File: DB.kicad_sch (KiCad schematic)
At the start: 20 parts

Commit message: Second Commit
new wiring and label
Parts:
- removed DBP0: Conn_01x11_Pin, symbol Connector:Conn_01x11_Pin
- removed DBP1 (x2): Conn_01x05_Pin, symbol Connector:Conn_01x05_Pin
- removed DBS0: Conn_01x11_Socket, Connector_Molex:Molex_PicoBlade_53261-1171_1x11-1MP_P1.25mm_Horizontal, symbol Connector:Conn_01x11_Socket
- removed DBS1: Conn_01x05_Socket, Connector_Molex:Molex_PicoBlade_53261-0571_1x05-1MP_P1.25mm_Horizontal, symbol Connector:Conn_01x05_Socket
- removed R1, R2 (x2): 5.1K, ScottoKeebs_Components:Resistor_0402, symbol Device:R_Small
- removed RK1: RotaryEncoder_Switch_MP, Rotary_Encoder:RotaryEncoder_Alps_EC11E-Switch_Vertical_H20mm, symbol Device:RotaryEncoder_Switch_MP
- removed SSW1 (x2): MSK13C01, Button_Switch_SMD:SW_SP3T_PCM13, symbol Switch:SW_SP3T
- removed SSW2 (x2): MSK12C01, Button_Switch_SMD:SW_SPDT_PCM12, symbol Switch:SW_SPDT
- removed USB1 (x2): USB_C_Receptacle_USB2.0_14P, ScottoKeebs_Components:USB_C_HRO_TYPE-C-31-M-12, symbol Connector:USB_C_Receptacle_USB2.0_14P
- added DBP1: Conn_01x05_Pin, symbol Connector:Conn_01x05_Pin
- added R2: 5.1K, ScottoKeebs_Components:Resistor_0402, symbol Device:R_Small
- added SSW1: MSK13C01, Button_Switch_SMD:SW_SP3T_PCM13, symbol Switch:SW_SP3T
- added SSW2: MSK12C01, Button_Switch_SMD:SW_SPDT_PCM12, symbol Switch:SW_SPDT
- added USB1: USB_C_Receptacle_USB2.0_14P, ScottoKeebs_Components:USB_C_HRO_TYPE-C-31-M-12, symbol Connector:USB_C_Receptacle_USB2.0_14P
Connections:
- net 2.4GHz Switch: now also SSW1.4
- net BT Switch: now also SSW1.1
- net COM Mode: now also SSW1.3
- net COM OS: now also SSW2.2 (B)
- net COM RK DBS: now also DBP1.3 (Pin_3)
- net GND: now also R2.2, USB1.A1 (GND), USB1.A12 (GND), USB1.B1 (GND), USB1.B12 (GND), USB1.S1 (SHIELD)
- net S1 RK DBS: now also DBP1.2 (Pin_2)
- net S2 RK DBS: now also DBP1.4 (Pin_4)
- net USB CC1: now also USB1.A5 (CC1)
- net USB CC2: now also R2.1, USB1.B5 (CC2)
- net USB D+: now also USB1.A6 (D+), USB1.B6 (D+)
- net USB D-: now also USB1.A7 (D-), USB1.B7 (D-)
- net VBUS: now also USB1.A4 (VBUS), USB1.A9 (VBUS), USB1.B4 (VBUS), USB1.B9 (VBUS)
- net VOL DOWN DBS: now also DBP1.1 (Pin_1)
- net VOL UP DBS: now also DBP1.5 (Pin_5)
- net Win: now also SSW2.1 (A)

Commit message: Third Commit
Kinda add some little changes but still confused on how using the nPM1300
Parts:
- removed RK1: RotaryEncoder_Switch_MP, Rotary_Encoder:RotaryEncoder_Alps_EC11E-Switch_Vertical_H20mm, symbol Device:RotaryEncoder_Switch_MP
- added RK1: RotaryEncoder_Switch_MP, HE_Keyswitch:RotaryEncoder_Bourns_Vertical_PEC11J-9220F-S0015, symbol HE_Keyswitch:RotaryEncoder_Switch_MP
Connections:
- net COM RK: now also RK1.C
- net S1 RK: now also DBS1.4 (Pin_4), RK1.D; no longer DBS1.2 (Pin_2)
- net S2 RK: now also DBS1.2 (Pin_2), RK1.E (S2); no longer DBS1.4 (Pin_4)
- net USB CC1: now also DBS0.9 (Pin_9); no longer DBS0.11 (Pin_11)
- net USB CC1 DBS: now also DBP0.9 (Pin_9); no longer DBP0.11 (Pin_11)
- net USB D+: now also DBS0.10 (Pin_10); no longer DBS0.9 (Pin_9)
- net USB D+ DBS: now also DBP0.10 (Pin_10); no longer DBP0.9 (Pin_9)
- net USB D-: now also DBS0.11 (Pin_11); no longer DBS0.10 (Pin_10)
- net USB D- DBS: now also DBP0.11 (Pin_11); no longer DBP0.10 (Pin_10)
- net VOL DOWN: now also RK1.B
- net VOL UP: now also RK1.A

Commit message: Fourth Commit
changing some name to not get sued :v
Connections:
- net USB CC1 DBS is gone; now on net Win DBS: DBP0.9 (Pin_9)
- net USB CC2 DBS is gone; now on net COM OS DBS: DBP0.8 (Pin_8)
- net COM OS: now also DBS0.8 (Pin_8); no longer DBS0.4 (Pin_4)
- net COM OS DBS: no longer DBP0.4 (Pin_4)
- net COM RK: now also DBS1.4 (Pin_4); no longer DBS1.3 (Pin_3)
- net COM RK DBS: now also DBP1.4 (Pin_4); no longer DBP1.3 (Pin_3)
- net GND: now also DBP0.4 (Pin_4), DBS0.4 (Pin_4); no longer DBP0.6 (Pin_6), DBS0.6 (Pin_6)
- net S1 RK: now also DBS1.2 (Pin_2); no longer DBS1.4 (Pin_4)
- net S2 RK: now also DBS1.1 (Pin_1); no longer DBS1.2 (Pin_2)
- net S2 RK DBS: now also DBP1.1 (Pin_1); no longer DBP1.4 (Pin_4)
- net USB CC1: now also DBS0.7 (Pin_7); no longer DBS0.9 (Pin_9)
- net USB CC2: now also DBS0.6 (Pin_6); no longer DBS0.8 (Pin_8)
- net VBUS: now also DBS0.5 (Pin_5); no longer DBS0.7 (Pin_7)
- net VBUS DBS: now also DBP0.5 (Pin_5); no longer DBP0.7 (Pin_7)
- net VOL DOWN: now also DBS1.5 (Pin_5); no longer DBS1.1 (Pin_1)
- net VOL DOWN DBS: now also DBP1.5 (Pin_5); no longer DBP1.1 (Pin_1)
- net VOL UP: now also DBS1.3 (Pin_3); no longer DBS1.5 (Pin_5)
- net VOL UP DBS: now also DBP1.3 (Pin_3); no longer DBP1.5 (Pin_5)
- net Win: now also DBS0.9 (Pin_9); no longer DBS0.5 (Pin_5)
- net Win DBS: no longer DBP0.5 (Pin_5)
- net USB D+ DBS renamed D+ DBS
- net USB D- DBS renamed D- DBS
- new net CC1 DBS: DBP0.7 (Pin_7)
- new net CC2 DBS: DBP0.6 (Pin_6)

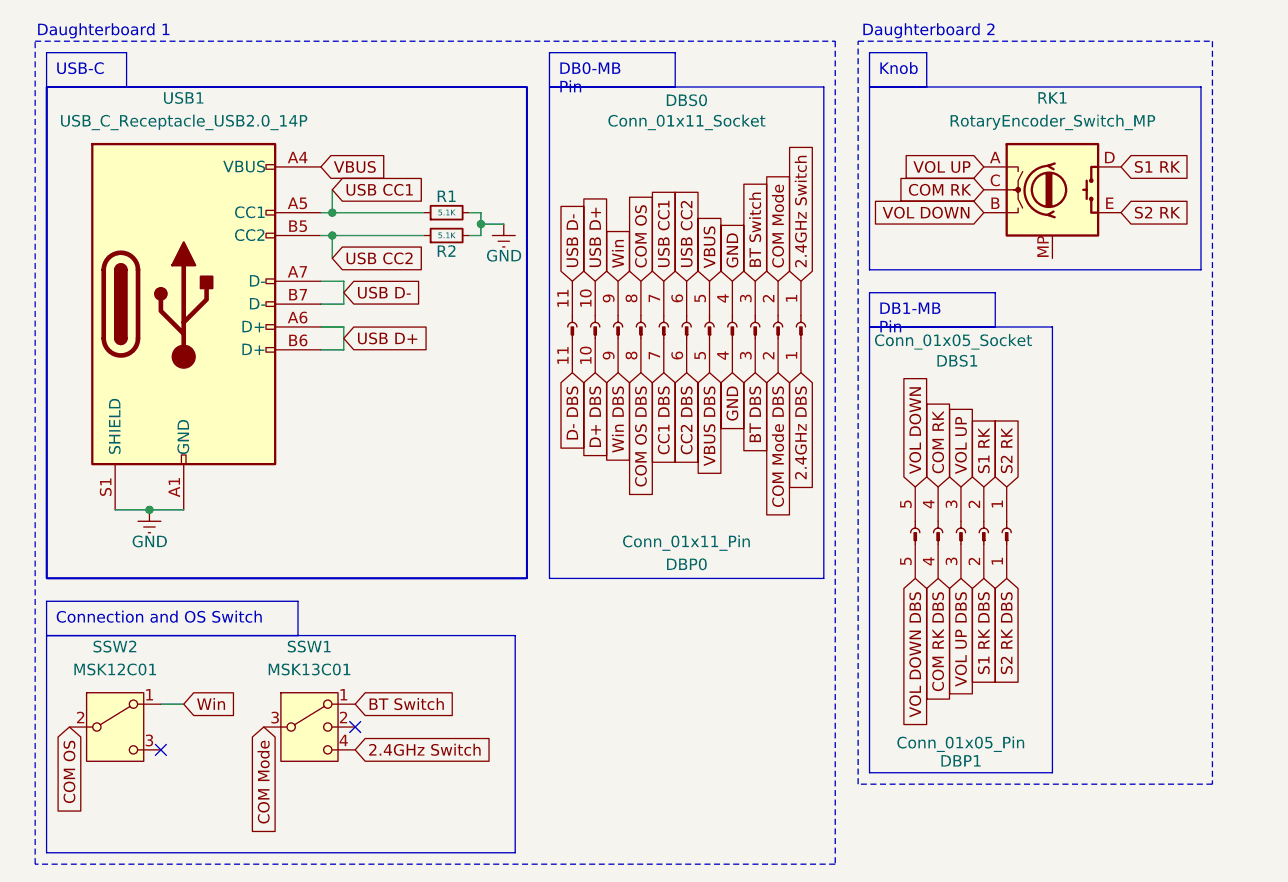
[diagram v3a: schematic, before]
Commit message: Fifth Commit
updating track width and via's diameter
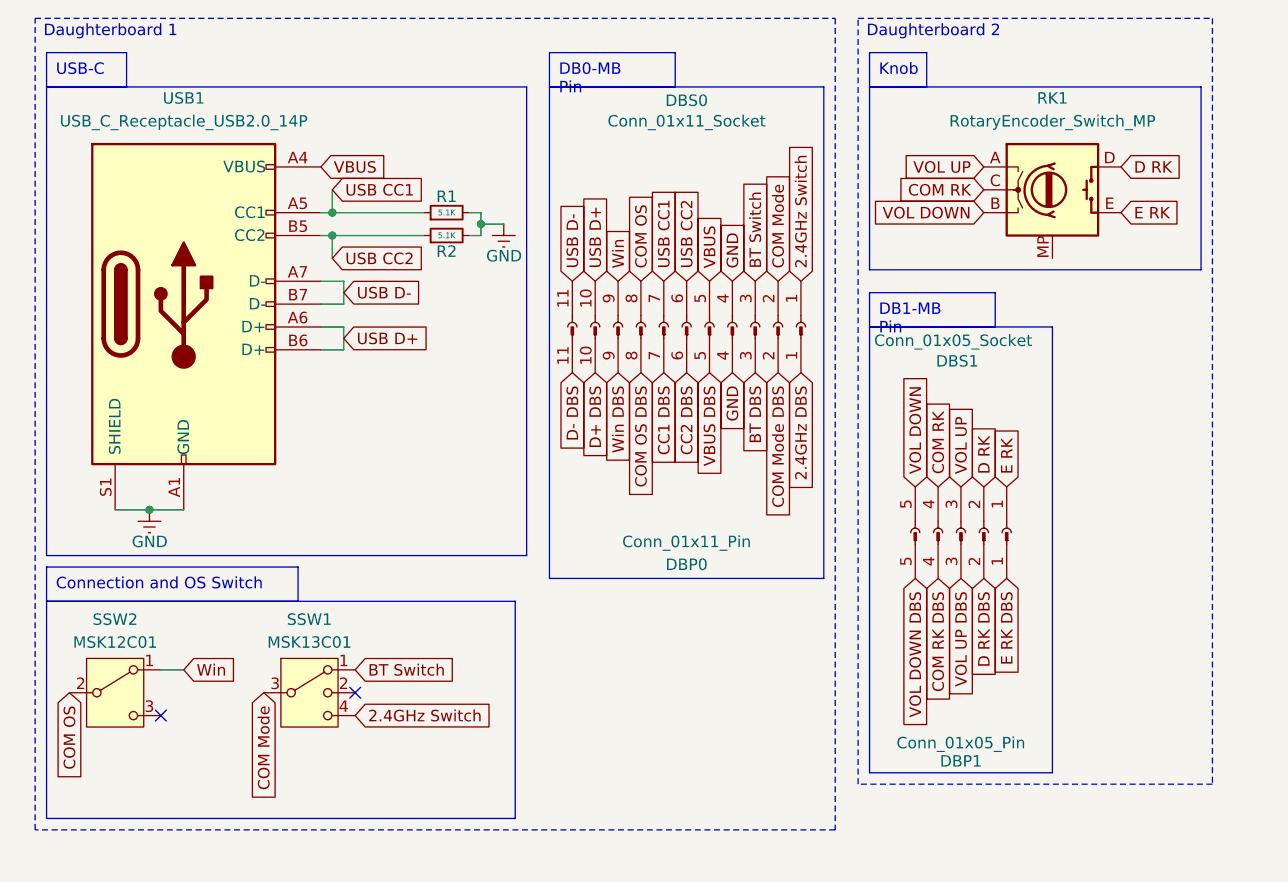
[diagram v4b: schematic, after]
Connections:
- net S1 RK renamed D RK
- net S1 RK DBS renamed D RK DBS
- net S2 RK renamed E RK
- net S2 RK DBS renamed E RK DBS
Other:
- moved on the sheet: SSW1, SSW2

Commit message: Sixth Commit
Almost done. Just need to make sure the field zone and each pin is connected properly
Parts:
- removed R1, R2: 5.1K, ScottoKeebs_Components:Resistor_0402, symbol Device:R_Small
- J1: renamed from USB1; symbol Connector:USB_C_Receptacle_USB2.0_14P -> HE_Keyswitch:USB_C_Receptacle_USB2.0_14P
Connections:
- net COM RK is gone; now on net GND: DBS1.4 (Pin_4), RK1.C
- net E RK is gone; now on net GND: DBS1.1 (Pin_1), RK1.E (S2)
- net VBUS DBS is gone; now on net CC2 DBS: DBP0.5 (Pin_5)
- net CC1 DBS: now also DBP0.6 (Pin_6); no longer DBP0.7 (Pin_7)
- net CC2 DBS: no longer DBP0.6 (Pin_6)
- net USB CC1: now also DBS0.6 (Pin_6); no longer DBS0.7 (Pin_7)
- net USB CC2: now also DBS0.5 (Pin_5); no longer DBS0.6 (Pin_6)
- net VBUS: now also DBP0.7 (Pin_7), DBS0.7 (Pin_7); no longer DBS0.5 (Pin_5)
- net MP: now reaches RK1.MP
- net D+ DBS renamed DBS D+
- net D- DBS renamed DBS D-
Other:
- moved on the sheet: DBP0, DBP1, DBS0, DBS1, J1, RK1, SSW1, SSW2

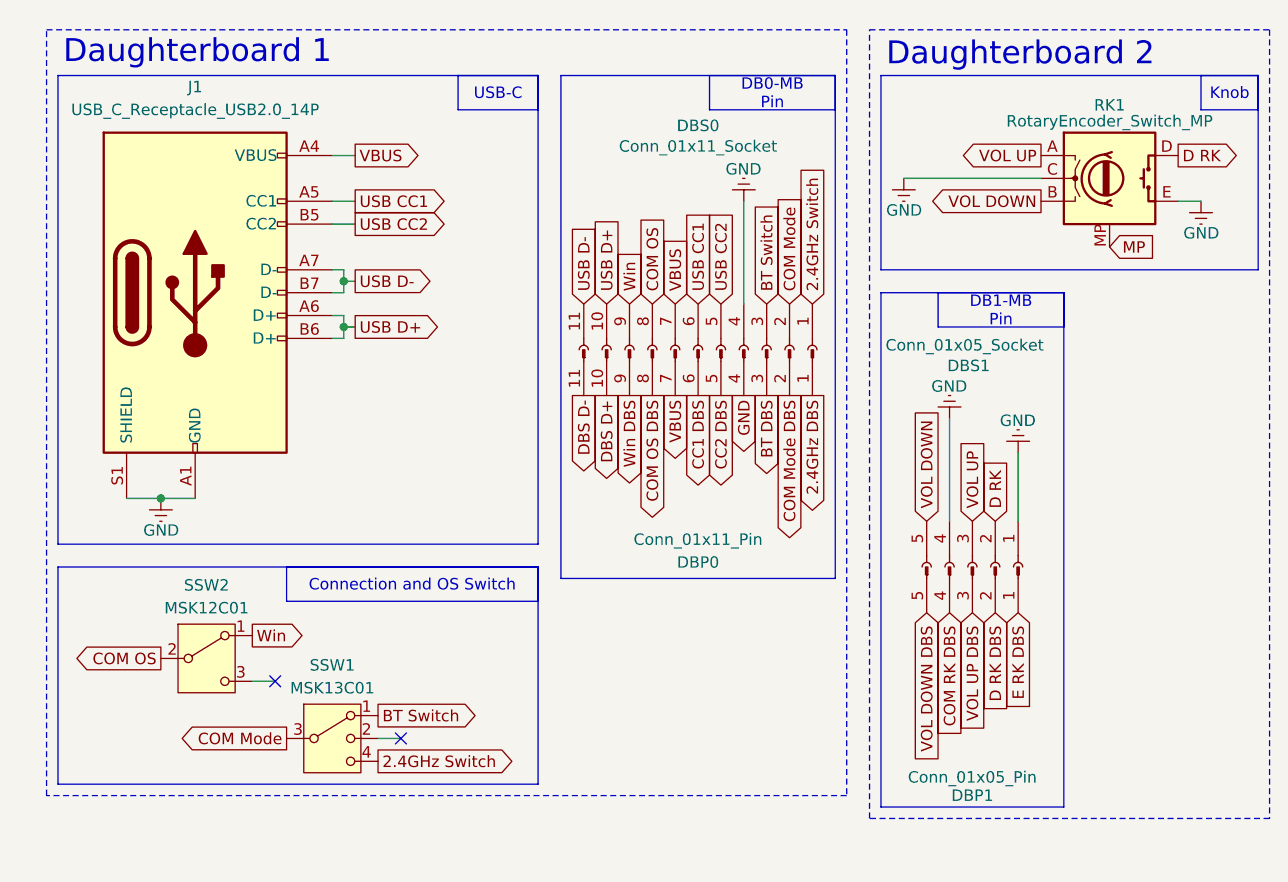
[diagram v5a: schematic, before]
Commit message: 7th Commit
Adding the reduced nRF52840 dongle and some minor tweak
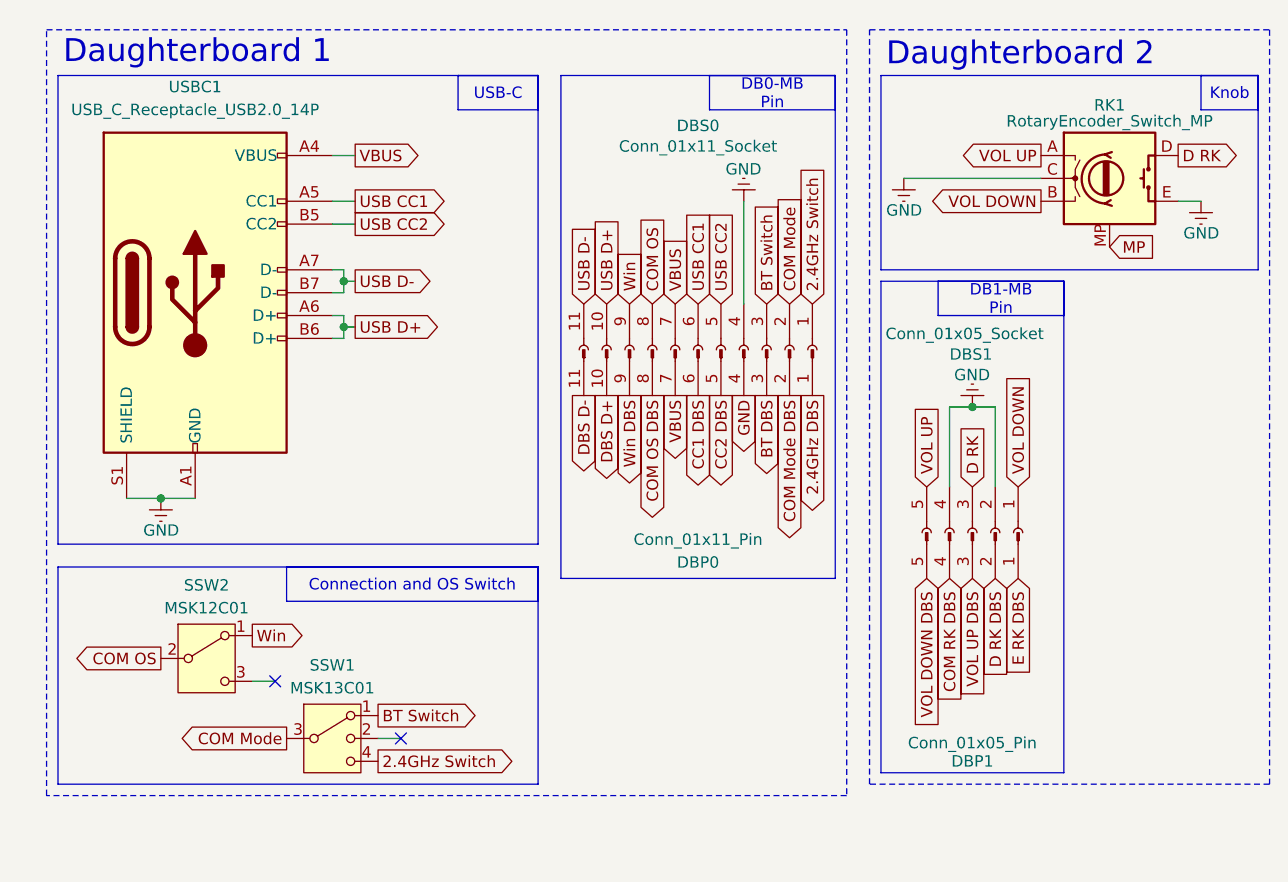
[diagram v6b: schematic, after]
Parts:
- renumbered J1 to USBC1
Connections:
- net D RK: now also DBS1.3 (Pin_3); no longer DBS1.2 (Pin_2)
- net GND: now also DBS1.2 (Pin_2); no longer DBS1.1 (Pin_1)
- net VOL DOWN: now also DBS1.1 (Pin_1); no longer DBS1.5 (Pin_5)
- net VOL UP: now also DBS1.5 (Pin_5); no longer DBS1.3 (Pin_3)
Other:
- moved on the sheet: DBP1, DBS1

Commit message: 8th commit
Some minor tweak
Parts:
- removed DBP0: Conn_01x11_Pin, symbol Connector:Conn_01x11_Pin
- removed DBP1: Conn_01x05_Pin, symbol Connector:Conn_01x05_Pin
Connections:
- net VBUS renamed VBUS USBC

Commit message: 9th commit
some minor tweak + adding production files
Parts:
- DBS0: value Conn_01x11_Socket -> HCZZ0001-11; footprint Connector_Molex:Molex_PicoBlade_53261-1171_1x11-1MP_P1.25mm_Horizontal -> HE_Keyswitch:Hong_Cheng_HCZZ0001-11; LCSC Part (none) -> C7433462
- DBS1: value Conn_01x05_Socket -> HCZZ0001-5; footprint Connector_Molex:Molex_PicoBlade_53261-0571_1x05-1MP_P1.25mm_Horizontal -> HE_Keyswitch:Hong_Cheng_HCZZ0001-5; LCSC Part (none) -> C7433456
- RK1: footprint HE_Keyswitch:RotaryEncoder_Bourns_Vertical_PEC11J-9220F-S0015 -> HE_Keyswitch:RotaryEncoder_CTR_ED11601M-FB15A7.0-C15-202; LCSC Part (none) -> C470592
- SSW1: value MSK13C01 -> K3-1346S-K1; footprint Button_Switch_SMD:SW_SP3T_PCM13 -> HE_Keyswitch:SW_SP3T_Korean_Hroparts_Elec_K3-1346S-K1; LCSC Part (none) -> C128957
- SSW2: value MSK12C01 -> K3-1280S-K1; footprint Button_Switch_SMD:SW_SPDT_PCM12 -> HE_Keyswitch:SW_SPDT_Korean_Hroparts_Elec_K3-1280S-K1; LCSC Part (none) -> C128953
- USBC1: LCSC Part (none) -> C165948
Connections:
- net COM OS is gone; now on net 3.3V: DBS0.8 (Pin_8), SSW2.2 (B)
- net COM Mode renamed 3.3V
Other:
- moved on the sheet: DBS1, RK1, SSW1
